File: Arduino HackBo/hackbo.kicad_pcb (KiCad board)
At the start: 2 copper layers, 11 parts, among them IC1 ATMEGA168-A, P1 CONN_8, P2 CONN_6, P3 CONN_8, P4 CONN_6, X1 CRYSTAL

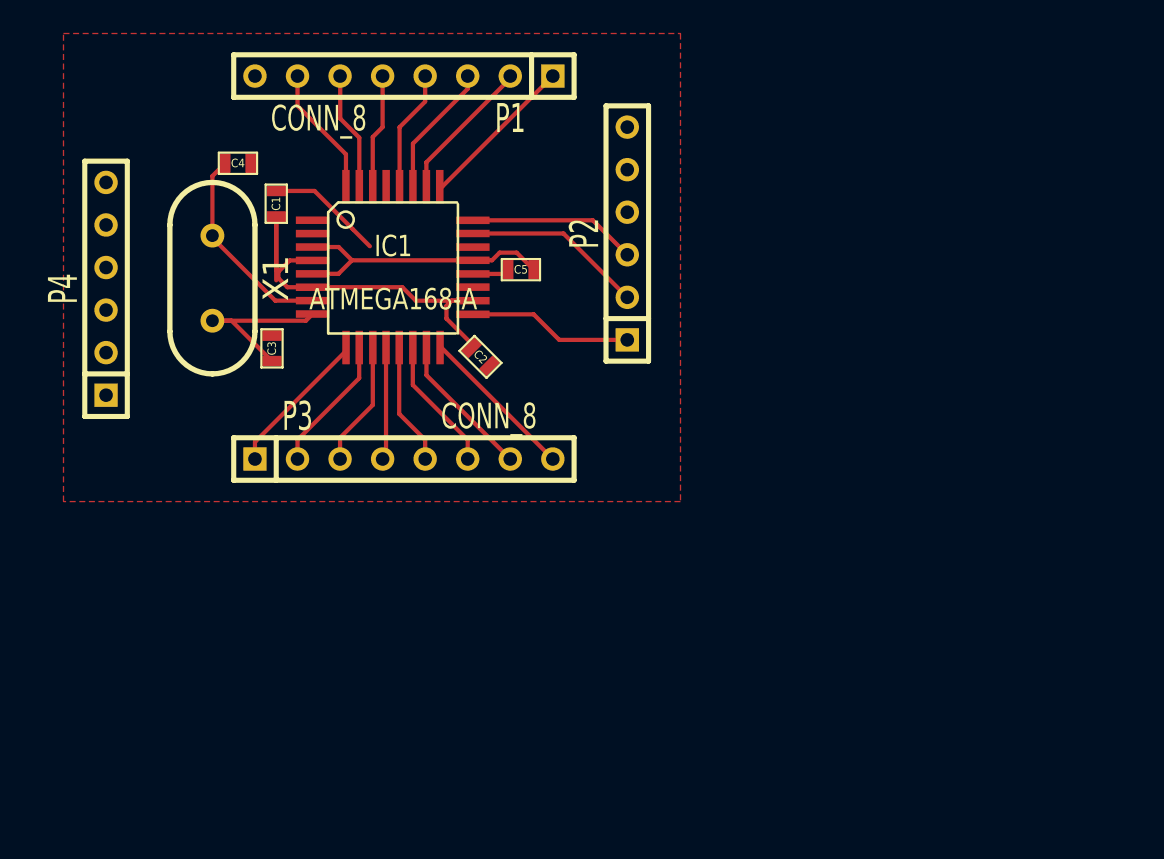
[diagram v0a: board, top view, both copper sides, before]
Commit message: Adicionado Reset y Alimentación (HackBo 2014-08-26)
- Se adicionó el circuito de reset y las conexiones para la
alimentación.
- Se eliminaron componentes no utilizados.
- Se generaron los archivos GERBER.
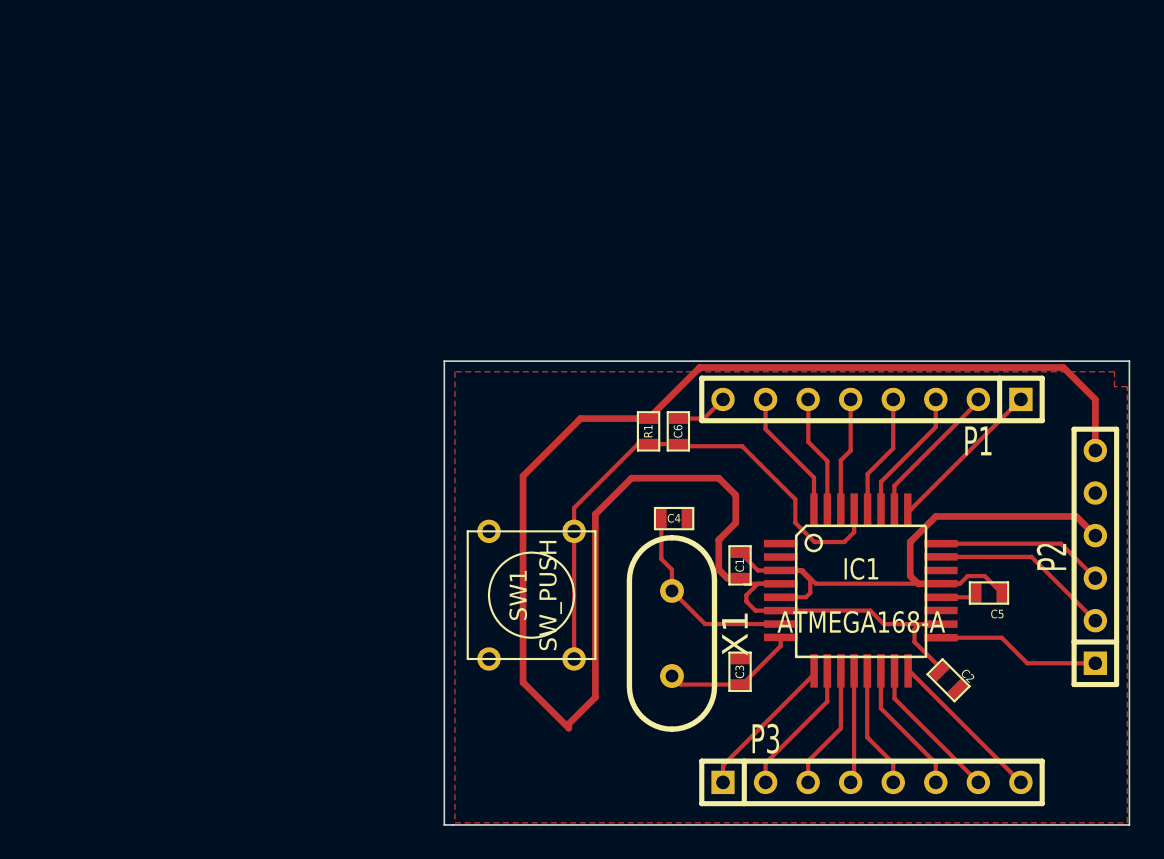
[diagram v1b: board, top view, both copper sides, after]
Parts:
- removed P4: CONN_6, SIL-6
- added C6: 0.1uF, SM0603, F.Cu at (57.0, 39.0)
- added R1: 10k, SM0603, F.Cu at (55.2, 39.0)
- added SW1: SW_PUSH, SW_PUSH_SMALL, F.Cu at (48.3, 48.8)
- moved C1 35.1 mm to (60.7, 47.0)
- moved X1 34.7 mm to (56.6, 51.1)
- moved C3 34.0 mm to (60.7, 53.3)
- moved P2 34.0 mm to (81.9, 46.5)
- moved C2 34.0 mm to (73.2, 53.8)
- moved C5 34.0 mm to (75.6, 48.6)
- moved IC1 34.0 mm to (67.9, 48.5)
- moved P1 34.0 mm to (68.6, 37.1)
- moved P3 34.0 mm to (68.6, 59.9)
- moved C4 33.6 mm to (56.8, 44.2)
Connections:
- IC1 pad 29: (no net) -> /Reset
- P1 pad 8: (no net) -> /DTR
- P2 pad 4: (no net) -> GND
- P2 pad 5: (no net) -> GND
- P2 pad 6: (no net) -> VCC
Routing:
- net VCC: track 26.9 -> 108.6 mm
- net /Reset: track 0.00 -> 32.3 mm
- net GND: track 23.8 -> 37.8 mm
- net /DTR: track 0.00 -> 3.14 mm
- net N-0000028: track 10.7 -> 8.16 mm
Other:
- board outline added: 40.9 x 27.7 mm
- net class POWER added: clearance 0.254, trace_width 0.4, via_dia 0.889, via_drill 0.635
- rule trace_min: 0.254 -> 0.2
